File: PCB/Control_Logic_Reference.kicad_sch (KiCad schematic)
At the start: 4 parts, among them U1 HC00, U2 HC08, U5 HC08, U7 HC00

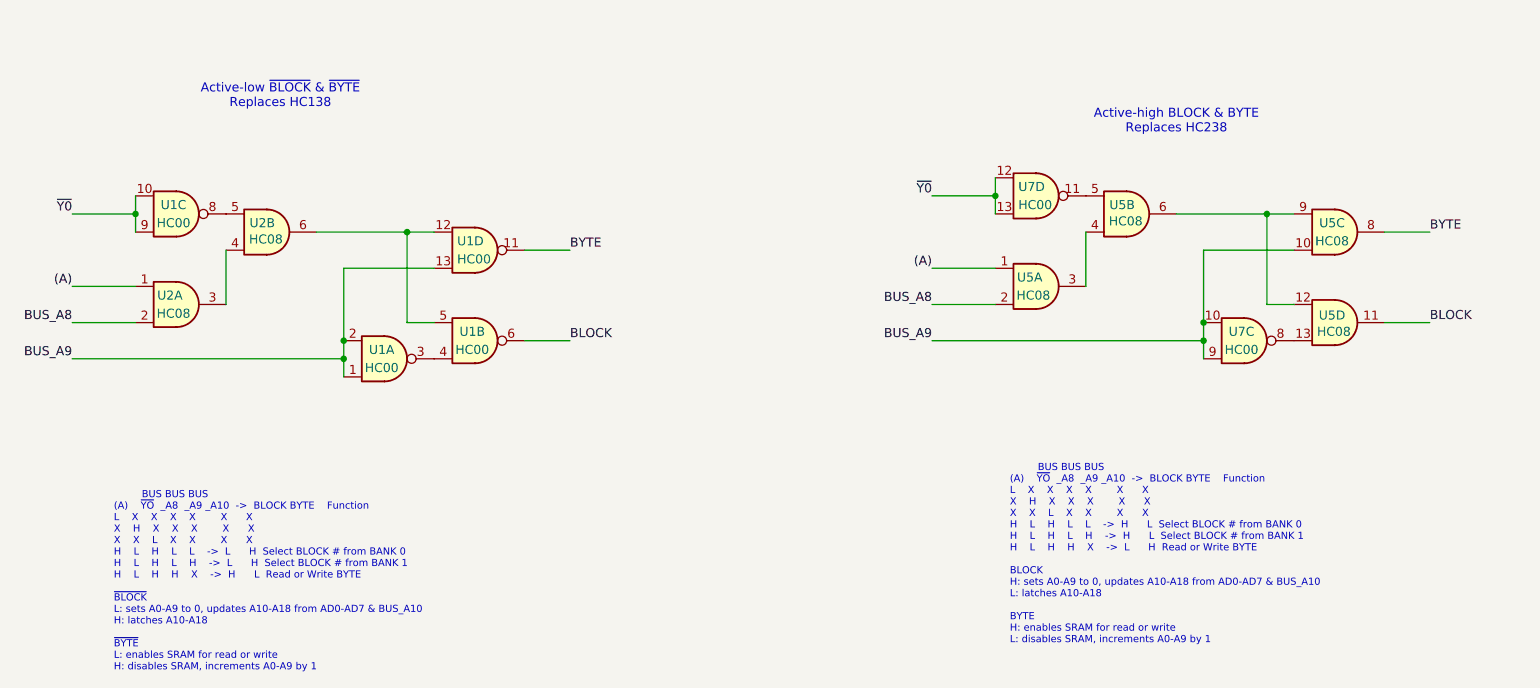
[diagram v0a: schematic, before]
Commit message: 512k G board - all large 1206 & soic
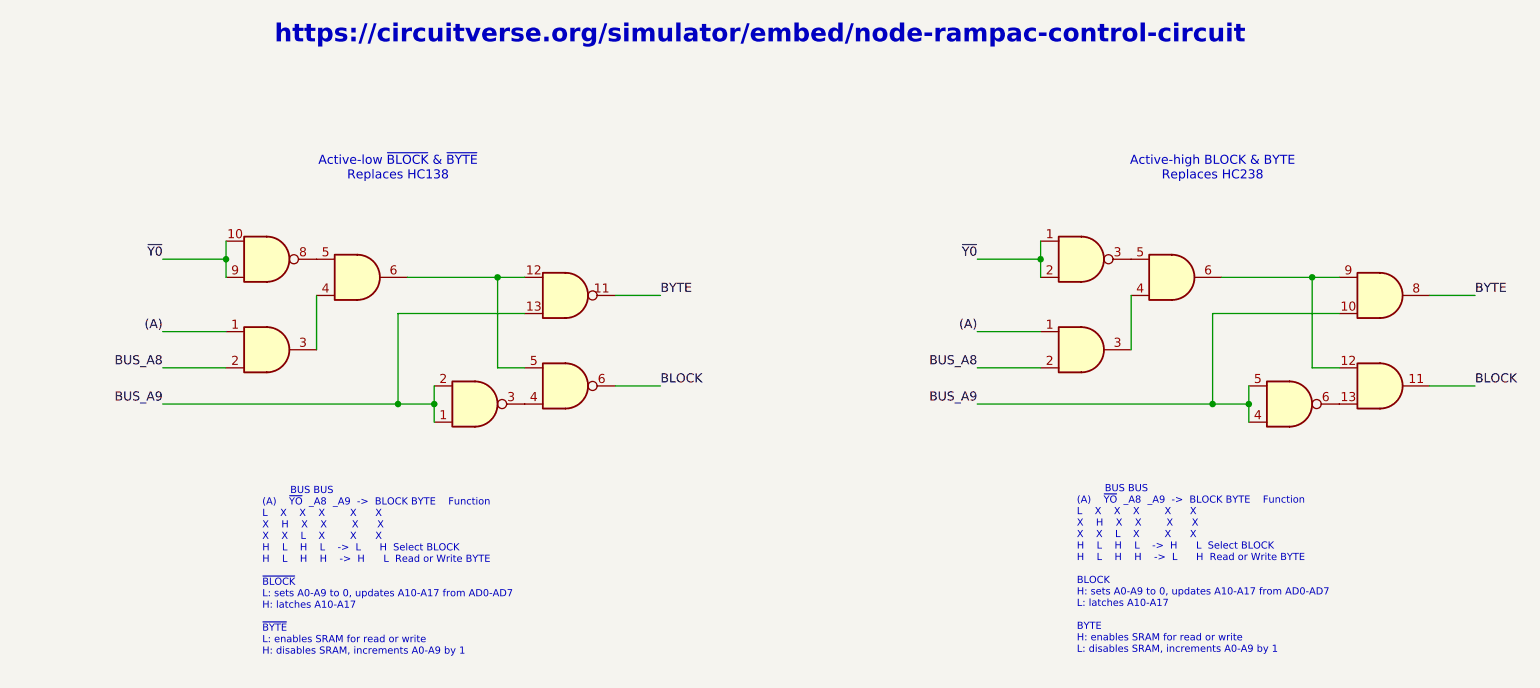
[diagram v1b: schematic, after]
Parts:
- renumbered U5 to U3, U7 to U4
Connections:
- net BUS_A9: now also U4.4, U4.5; no longer U4.10, U4.9
- net ~{Y0}: now also U4.1, U4.2; no longer U4.12, U4.13
- net at U3.5: now also U4.3; no longer U4.11
- net at U3.13: now also U4.6; no longer U4.8
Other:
- note added: "BUS BUS (A) ~{YO} _A8 _A9 -> BLOCK BYTE Function L X X X X X X H X X X X X X L X X X H L H L -> H L Select BLOCK H L H H -> L H Read or Write BYTE BLOCK H: sets A0-A9 to 0, updates A10-A17 from AD0-AD7 L: latches A10-A17 BYTE H: enables SRAM for read or write L: disables SRAM, increments A0-A9 by 1"
- note added: "BUS BUS (A) ~{YO} _A8 _A9 -> BLOCK BYTE Function L X X X X X X H X X X X X X L X X X H L H L -> L H Select BLOCK H L H H -> H L Read or Write BYTE ~{BLOCK} L: sets A0-A9 to 0, updates A10-A17 from AD0-AD7 H: latches A10-A17 ~{BYTE} L: enables SRAM for read or write H: disables SRAM, increments A0-A9 by 1"
- note added: "https://circuitverse.org/simulator/embed/node-rampac-control-circuit"
- note removed: "BUS BUS BUS (A) ~{YO} _A8 _A9 _A10 -> BLOCK BYTE Function L X X X X X X X H X X X X X X X L X X X X H L H L L -> H L Select BLOCK # from BANK 0 H L H L H -> H L Select BLOCK # from BANK 1 H L H H X -> L H Read or Write BYTE BLOCK H: sets A0-A9 to 0, updates A10-A18 from AD0-AD7 & BUS_A10 L: latches A10-A18 BYTE H: enables SRAM for read or write L: disables SRAM, increments A0-A9 by 1"
- note removed: "BUS BUS BUS (A) ~{YO} _A8 _A9 _A10 -> BLOCK BYTE Function L X X X X X X X H X X X X X X X L X X X X H L H L L -> L H Select BLOCK # from BANK 0 H L H L H -> L H Select BLOCK # from BANK 1 H L H H X -> H L Read or Write BYTE ~{BLOCK} L: sets A0-A9 to 0, updates A10-A18 from AD0-AD7 & BUS_A10 H: latches A10-A18 ~{BYTE} L: enables SRAM for read or write H: disables SRAM, increments A0-A9 by 1"
- title: MiniNDP control circuit - active high output -> RAMPAC Control Logic
